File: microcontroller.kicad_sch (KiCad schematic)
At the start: 22 parts, among them J1 TC2030-IDC, U1 ESP32-WROVER

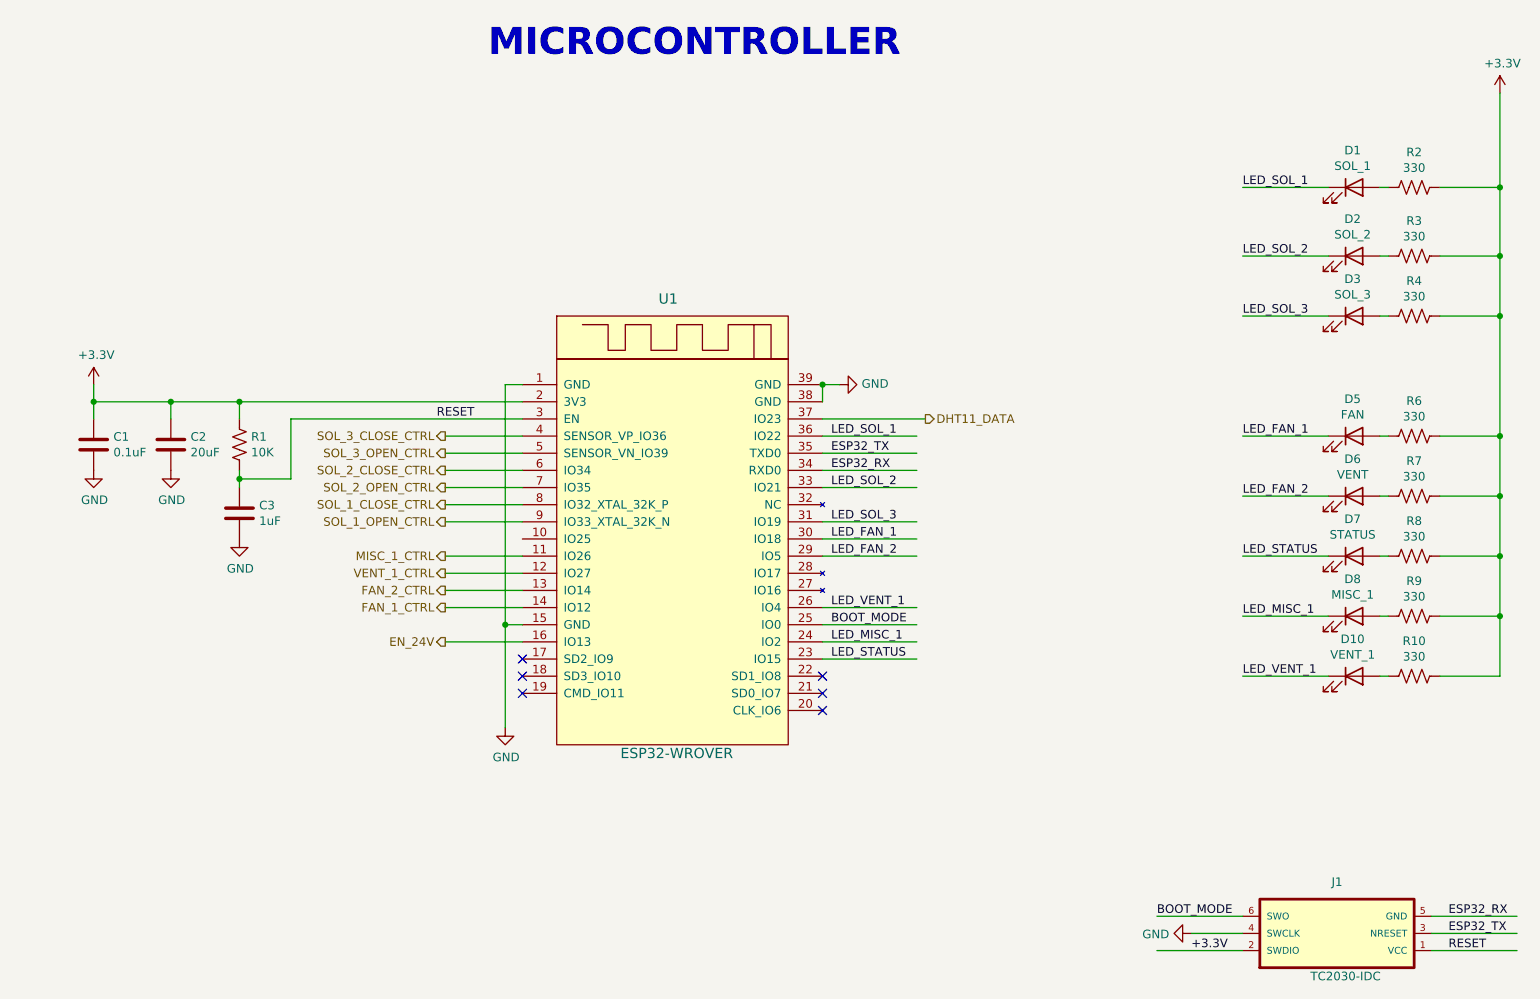
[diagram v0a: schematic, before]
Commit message: Added connector for temperature sensor. Started to route board.
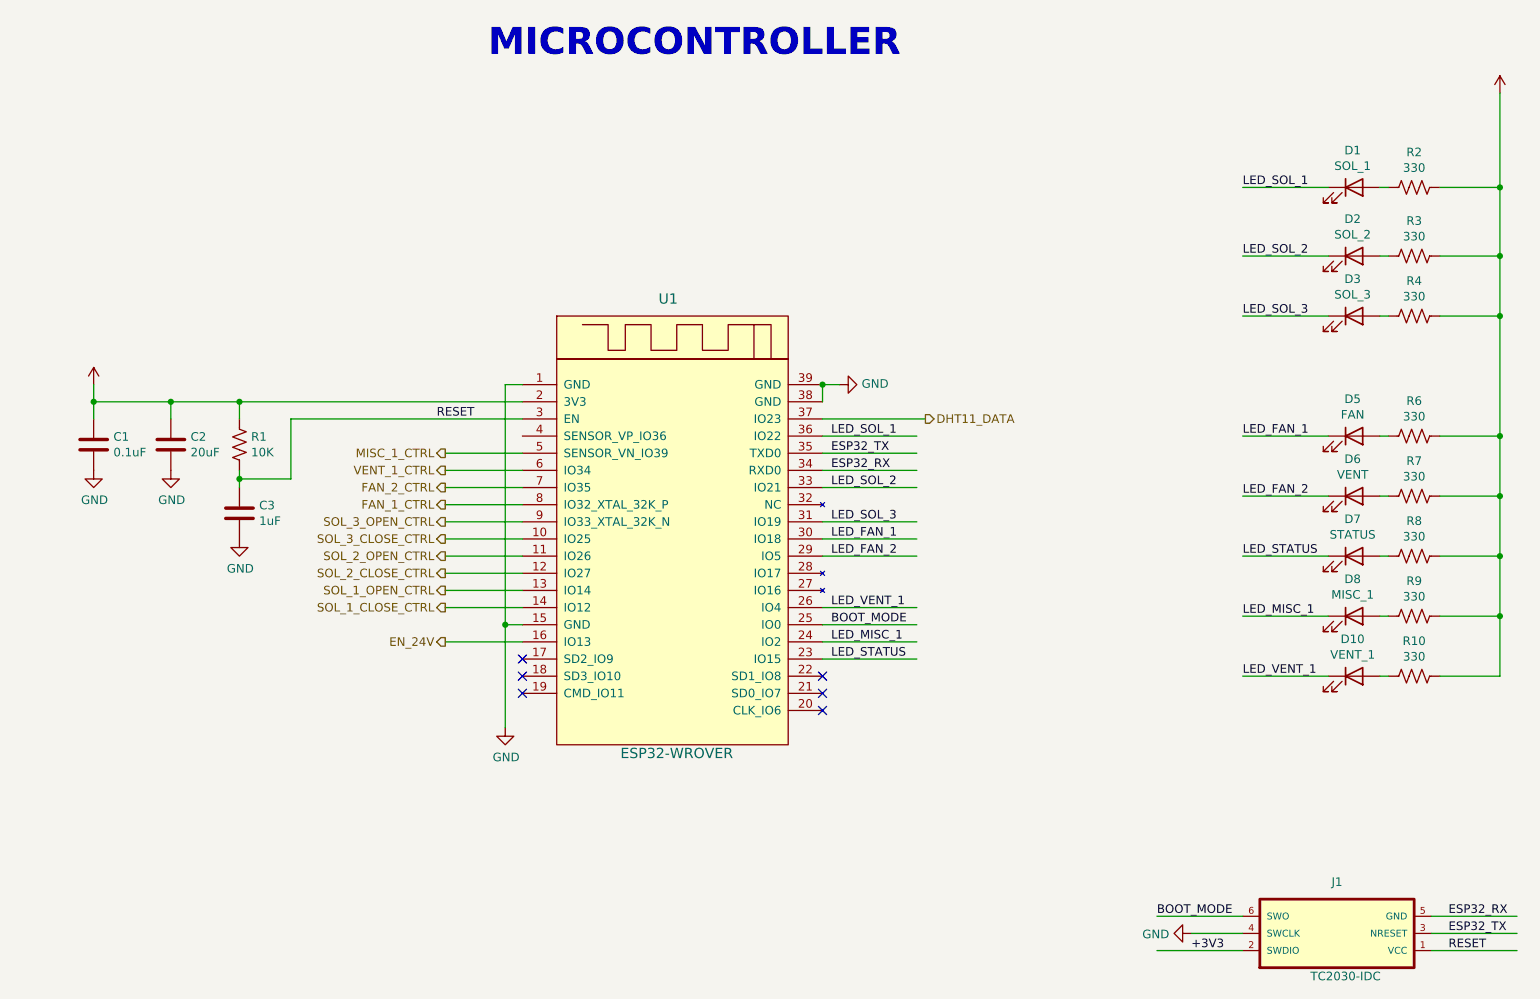
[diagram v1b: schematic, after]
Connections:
- net +3.3V is gone; now on net +3V3: J1.2 (SWDIO)
- net FAN_1_CTRL: now also U1.8 (IO32_XTAL_32K_P); no longer U1.14 (IO12)
- net FAN_2_CTRL: now also U1.7 (IO35); no longer U1.13 (IO14)
- net MISC_1_CTRL: now also U1.5 (SENSOR_VN_IO39); no longer U1.11 (IO26)
- net SOL_1_CLOSE_CTRL: now also U1.14 (IO12); no longer U1.8 (IO32_XTAL_32K_P)
- net SOL_1_OPEN_CTRL: now also U1.13 (IO14); no longer U1.9 (IO33_XTAL_32K_N)
- net SOL_2_CLOSE_CTRL: now also U1.12 (IO27); no longer U1.6 (IO34)
- net SOL_2_OPEN_CTRL: now also U1.11 (IO26); no longer U1.7 (IO35)
- net SOL_3_CLOSE_CTRL: now also U1.10 (IO25); no longer U1.4 (SENSOR_VP_IO36)
- net SOL_3_OPEN_CTRL: now also U1.9 (IO33_XTAL_32K_N); no longer U1.5 (SENSOR_VN_IO39)
- net VENT_1_CTRL: now also U1.6 (IO34); no longer U1.12 (IO27)
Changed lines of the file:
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@@
   (junction (at 88.9 87.63) (diameter 0) (color 0 0 0 0)
   )
+  (junction (at 78.74 76.2) (diameter 0) (color 0 0 0 0)
+  )
   (junction (at 275.59 63.5) (diameter 0) (color 0 0 0 0)
   )
-  (junction (at 78.74 76.2) (diameter 0) (color 0 0 0 0)
+  (junction (at 275.59 44.45) (diameter 0) (color 0 0 0 0)
   )
   (junction (at 88.9 76.2) (diameter 0) (color 0 0 0 0)
   )
-  (junction (at 275.59 44.45) (diameter 0) (color 0 0 0 0)
+  (junction (at 67.31 76.2) (diameter 0) (color 0 0 0 0)
   )
   (junction (at 275.59 99.06) (diameter 0) (color 0 0 0 0)
   )
   (junction (at 275.59 54.61) (diameter 0) (color 0 0 0 0)
-  )
-  (junction (at 67.31 76.2) (diameter 0) (color 0 0 0 0)
   )
   (junction (at 275.59 81.28) (diameter 0) (color 0 0 0 0)
@@
     (stroke (width 0) (type default) (color 0 0 0 0))
   )
+  (wire (pts (xy 67.31 76.2) (xy 67.31 78.74))
+    (stroke (width 0) (type default) (color 0 0 0 0))
+  )
   (wire (pts (xy 175.26 99.06) (xy 189.23 99.06))
     (stroke (width 0) (type default) (color 0 0 0 0))
@@
     (stroke (width 0) (type default) (color 0 0 0 0))
   )
+  (wire (pts (xy 78.74 76.2) (xy 78.74 78.74))
+    (stroke (width 0) (type default) (color 0 0 0 0))
+  )
   (wire (pts (xy 130.81 104.14) (xy 119.38 104.14))
     (stroke (width 0) (type default) (color 0 0 0 0))
@@
     (stroke (width 0) (type default) (color 0 0 0 0))
   )
-  (wire (pts (xy 88.9 76.2) (xy 130.81 76.2))
-    (stroke (width 0) (type default) (color 0 0 0 0))
-  )
   (wire (pts (xy 250.19 90.17) (xy 237.49 90.17))
     (stroke (width 0) (type default) (color 0 0 0 0))
   )
-  (wire (pts (xy 119.38 81.28) (xy 130.81 81.28))
-    (stroke (width 0) (type default) (color 0 0 0 0))
-  )
-  (wire (pts (xy 78.74 78.74) (xy 78.74 76.2))
+  (wire (pts (xy 130.81 76.2) (xy 88.9 76.2))
     (stroke (width 0) (type default) (color 0 0 0 0))
   )
@@
     (stroke (width 0) (type default) (color 0 0 0 0))
   )
-  (wire (pts (xy 78.74 76.2) (xy 88.9 76.2))
-    (stroke (width 0) (type default) (color 0 0 0 0))
-  )
-  (wire (pts (xy 88.9 78.74) (xy 88.9 76.2))
-    (stroke (width 0) (type default) (color 0 0 0 0))
-  )
   (wire (pts (xy 265.43 154.94) (xy 278.13 154.94))
     (stroke (width 0) (type default) (color 0 0 0 0))
@@
     (stroke (width 0) (type default) (color 0 0 0 0))
   )
-  (wire (pts (xy 67.31 76.2) (xy 67.31 78.74))
-    (stroke (width 0) (type default) (color 0 0 0 0))
-  )
   (wire (pts (xy 250.19 44.45) (xy 237.49 44.45))
     (stroke (width 0) (type default) (color 0 0 0 0))
@@
     (stroke (width 0) (type default) (color 0 0 0 0))
   )
+  (wire (pts (xy 88.9 76.2) (xy 78.74 76.2))
+    (stroke (width 0) (type default) (color 0 0 0 0))
+  )
+  (wire (pts (xy 78.74 76.2) (xy 67.31 76.2))
+    (stroke (width 0) (type default) (color 0 0 0 0))
+  )
   (wire (pts (xy 237.49 152.4) (xy 224.79 152.4))
     (stroke (width 0) (type default) (color 0 0 0 0))
@@
     (stroke (width 0) (type default) (color 0 0 0 0))
   )
-  (wire (pts (xy 67.31 76.2) (xy 67.31 73.66))
+  (wire (pts (xy 119.38 96.52) (xy 130.81 96.52))
     (stroke (width 0) (type default) (color 0 0 0 0))
   )
@@
     (stroke (width 0) (type default) (color 0 0 0 0))
   )
+  (wire (pts (xy 67.31 73.66) (xy 67.31 76.2))
+    (stroke (width 0) (type default) (color 0 0 0 0))
+  )
   (wire (pts (xy 130.81 106.68) (xy 119.38 106.68))
     (stroke (width 0) (type default) (color 0 0 0 0))
@@
     (stroke (width 0) (type default) (color 0 0 0 0))
   )
-  (wire (pts (xy 67.31 76.2) (xy 78.74 76.2))
+  (wire (pts (xy 88.9 76.2) (xy 88.9 78.74))
     (stroke (width 0) (type default) (color 0 0 0 0))
   )
@@
     (effects (font (size 1.27 1.27)) (justify left bottom))
   )
-  (label "+3.3V" (at 229.87 157.48 0)
+  (label "+3V3" (at 229.87 157.48 0)
     (effects (font (size 1.27 1.27)) (justify left bottom))
   )
@@
   (label "LED_SOL_1" (at 176.53 81.28 0)
     (effects (font (size 1.27 1.27)) (justify left bottom))
+  )
+  (hierarchical_label "SOL_3_CLOSE_CTRL" (shape output) (at 119.38 96.52 180)
+    (effects (font (size 1.27 1.27)) (justify right))
   )
   (hierarchical_label "DHT11_DATA" (shape output) (at 190.5 78.74 0)
     (effects (font (size 1.27 1.27)) (justify left))
   )
+  (hierarchical_label "VENT_1_CTRL" (shape output) (at 119.38 86.36 180)
+    (effects (font (size 1.27 1.27)) (justify right))
+  )
+  (hierarchical_label "FAN_2_CTRL" (shape output) (at 119.38 88.9 180)
+    (effects (font (size 1.27 1.27)) (justify right))
+  )
   (hierarchical_label "EN_24V" (shape output) (at 119.38 111.76 180)
     (effects (font (size 1.27 1.27)) (justify right))
   )
-  (hierarchical_label "SOL_1_OPEN_CTRL" (shape output) (at 119.38 93.98 180)
-    (effects (font (size 1.27 1.27)) (justify right))
-  )
-  (hierarchical_label "MISC_1_CTRL" (shape output) (at 119.38 99.06 180)
-    (effects (font (size 1.27 1.27)) (justify right))
-  )
-  (hierarchical_label "SOL_1_CLOSE_CTRL" (shape output) (at 119.38 91.44 180)
-    (effects (font (size 1.27 1.27)) (justify right))
-  )
-  (hierarchical_label "FAN_2_CTRL" (shape output) (at 119.38 104.14 180)
-    (effects (font (size 1.27 1.27)) (justify right))
-  )
-  (hierarchical_label "SOL_3_CLOSE_CTRL" (shape output) (at 119.38 81.28 180)
-    (effects (font (size 1.27 1.27)) (justify right))
-  )
-  (hierarchical_label "FAN_1_CTRL" (shape output) (at 119.38 106.68 180)
-    (effects (font (size 1.27 1.27)) (justify right))
-  )
-  (hierarchical_label "SOL_3_OPEN_CTRL" (shape output) (at 119.38 83.82 180)
-    (effects (font (size 1.27 1.27)) (justify right))
-  )
-  (hierarchical_label "SOL_2_CLOSE_CTRL" (shape output) (at 119.38 86.36 180)
-    (effects (font (size 1.27 1.27)) (justify right))
-  )
-  (hierarchical_label "SOL_2_OPEN_CTRL" (shape output) (at 119.38 88.9 180)
-    (effects (font (size 1.27 1.27)) (justify right))
-  )
-  (hierarchical_label "VENT_1_CTRL" (shape output) (at 119.38 101.6 180)
-    (effects (font (size 1.27 1.27)) (justify right))
-  )
-  (symbol (lib_id "power:+3.3V") (at 67.31 73.66 0) (unit 1)
-    (in_bom yes) (on_board yes)
-    (property "Reference" "#PWR01" (id 0) (at 67.31 77.47 0)
-      (effects (font (size 1.27 1.27)) hide)
-    )
-    (property "Value" "+3.3V" (id 1) (at 67.691 69.2658 0))
-    (property "Footprint" "" (id 2) (at 67.31 73.66 0)
-      (effects (font (size 1.27 1.27)) hide)
-    )
-    (property "Datasheet" "" (id 3) (at 67.31 73.66 0)
-      (effects (font (size 1.27 1.27)) hide)
-    )
-    (pin "1")
+  (hierarchical_label "FAN_1_CTRL" (shape output) (at 119.38 91.44 180)
+    (effects (font (size 1.27 1.27)) (justify right))
+  )
+  (hierarchical_label "SOL_1_OPEN_CTRL" (shape output) (at 119.38 104.14 180)
+    (effects (font (size 1.27 1.27)) (justify right))
+  )
+  (hierarchical_label "SOL_2_CLOSE_CTRL" (shape output) (at 119.38 101.6 180)
+    (effects (font (size 1.27 1.27)) (justify right))
+  )
+  (hierarchical_label "MISC_1_CTRL" (shape output) (at 119.38 83.82 180)
+    (effects (font (size 1.27 1.27)) (justify right))
+  )
+  (hierarchical_label "SOL_2_OPEN_CTRL" (shape output) (at 119.38 99.06 180)
+    (effects (font (size 1.27 1.27)) (justify right))
+  )
+  (hierarchical_label "SOL_1_CLOSE_CTRL" (shape output) (at 119.38 106.68 180)
+    (effects (font (size 1.27 1.27)) (justify right))
+  )
+  (hierarchical_label "SOL_3_OPEN_CTRL" (shape output) (at 119.38 93.98 180)
+    (effects (font (size 1.27 1.27)) (justify right))
   )
   (symbol (lib_id "green_house_controller-rescue:ESP32-WROVER-esp32-wrover") (at 153.67 92.71 0) (unit 1)
@@
     (pin "1")
   )
-  (symbol (lib_id "power:+3.3V") (at 275.59 30.48 0) (unit 1)
-    (in_bom yes) (on_board yes)
-    (property "Reference" "#PWR0101" (id 0) (at 275.59 34.29 0)
-      (effects (font (size 1.27 1.27)) hide)
-    )
-    (property "Value" "+3.3V" (id 1) (at 275.971 26.0858 0))
-    (property "Footprint" "" (id 2) (at 275.59 30.48 0)
-      (effects (font (size 1.27 1.27)) hide)
-    )
-    (property "Datasheet" "" (id 3) (at 275.59 30.48 0)
-      (effects (font (size 1.27 1.27)) hide)
-    )
-    (pin "1")
-  )
   (symbol (lib_id "Device:LED") (at 254 107.95 0) (unit 1)
     (in_bom yes) (on_board yes)
@@
     (pin "2")
   )
+  (symbol (lib_id "power:+3V3") (at 67.31 73.66 0) (unit 1)
+    (in_bom yes) (on_board yes) (fields_autoplaced)
+    (property "Reference" "#PWR0103" (id 0) (at 67.31 77.47 0)
+      (effects (font (size 1.27 1.27)) hide)
+    )
+    (property "Value" "" (id 1) (at 67.31 68.58 0))
+    (property "Footprint" "" (id 2) (at 67.31 73.66 0)
+      (effects (font (size 1.27 1.27)) hide)
+    )
+    (property "Datasheet" "" (id 3) (at 67.31 73.66 0)
+      (effects (font (size 1.27 1.27)) hide)
+    )
+    (pin "1")
+  )
+  (symbol (lib_id "power:+3V3") (at 275.59 30.48 0) (unit 1)
+    (in_bom yes) (on_board yes) (fields_autoplaced)
+    (property "Reference" "#PWR0101" (id 0) (at 275.59 34.29 0)
+      (effects (font (size 1.27 1.27)) hide)
+    )
+    (property "Value" "" (id 1) (at 275.59 25.4 0))
+    (property "Footprint" "" (id 2) (at 275.59 30.48 0)
+      (effects (font (size 1.27 1.27)) hide)
+    )
+    (property "Datasheet" "" (id 3) (at 275.59 30.48 0)
+      (effects (font (size 1.27 1.27)) hide)
+    )
+    (pin "1")
+  )
 )
